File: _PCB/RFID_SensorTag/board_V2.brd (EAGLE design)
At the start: 95 x 60 mm, 21 parts, among them J2 SMT, J3 SMT, U1 MAXIM_ELECTRONICS_MAX40200AUK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, X1 53048-02

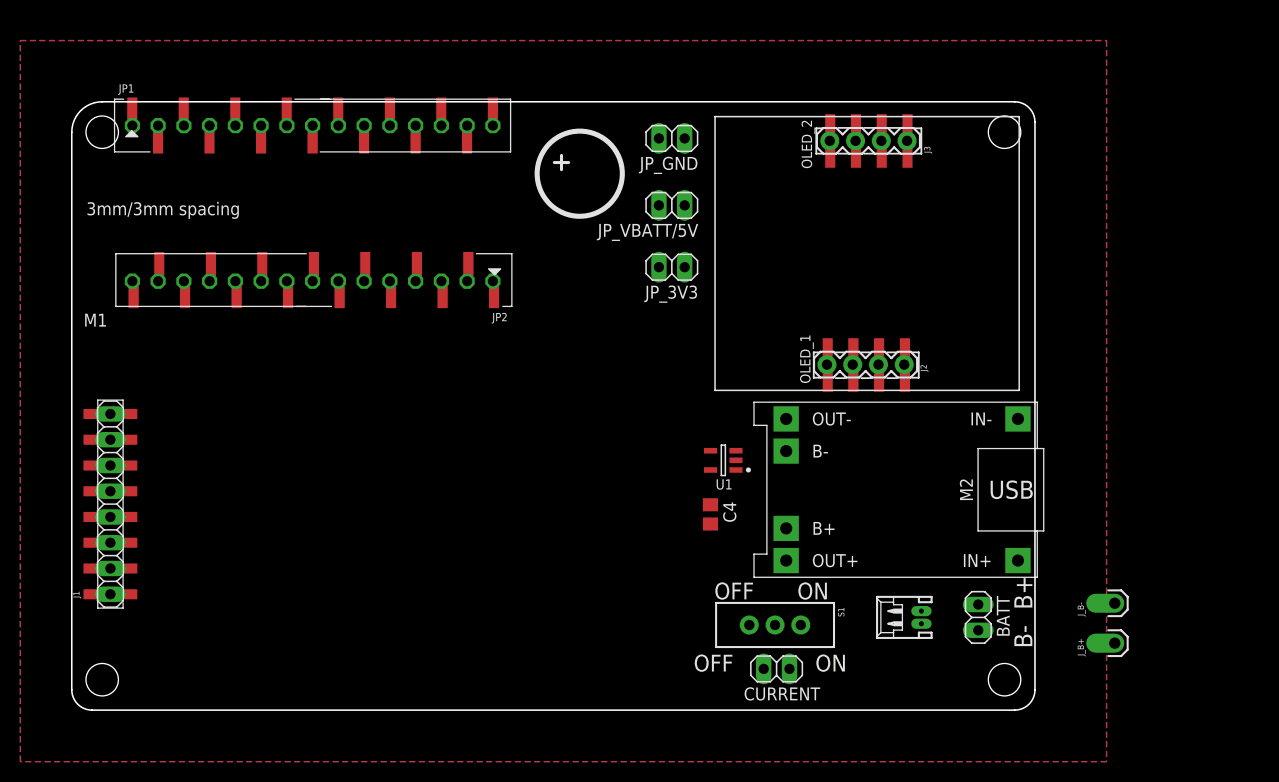
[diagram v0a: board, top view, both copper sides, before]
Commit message: RFID system V2 out
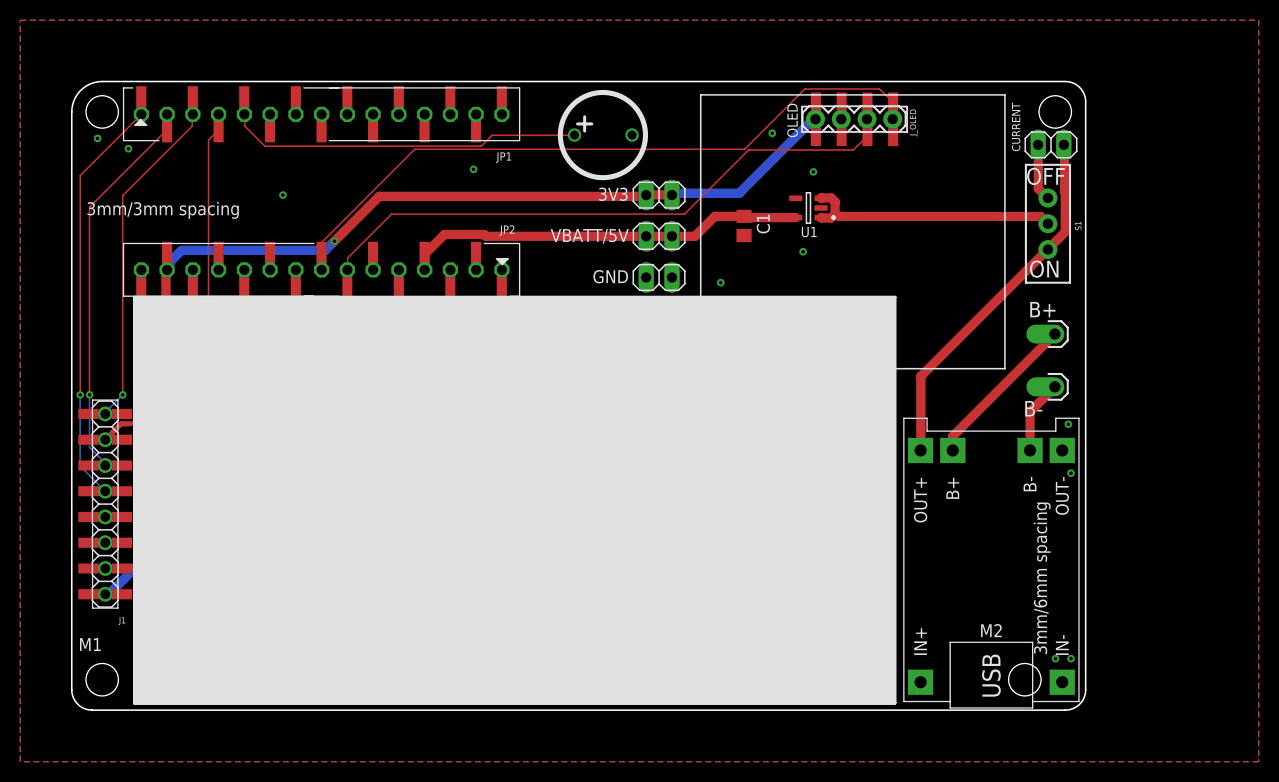
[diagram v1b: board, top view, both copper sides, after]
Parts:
- removed BATT, JP_3V3, JP_GND, JP_VBATT/5V: (no value), pinhead:1X02
- removed C4: 100nF, rcl:C0805
- removed J2, J3: SMT, SparkFun-Connectors:1X04_SMD_VERTICAL_COMBO
- removed J_B+, J_B-: (no value), SparkFun-Connectors:1X01_OFFSET
- removed OLED_1, OLED_2: (no value), SparkFun-Connectors:1X04
- removed X1: 53048-02, con-molex:53048-02
- added 3V3, GND, VBATT/5V: (no value), pinhead:1X02
- added B+, B-: (no value), SparkFun-Connectors:1X01_OFFSET
- added C1: 100nF, rcl:C0805
- added J_OLED: SMT, SparkFun-Connectors:1X04_SMD_VERTICAL_COMBO
- added OLED: (no value), SparkFun-Connectors:1X04
- moved CURRENT 58.3 mm to (96.6, 55.8)
- moved S1 47.9 mm to (96.3, 48.0), turned to 180 degrees
- moved U1 26.3 mm to (72.7, 49.5)
- moved M2 11.7 mm to (90.7, 14.8), turned to 90 degrees
- moved JP1 1.42 mm to (24.6, 58.8)
- moved U$1 1.42 mm to (33.5, 53.6)
- moved JP2 1.26 mm to (24.6, 43.4)
- moved J1 0.51 mm to (3.30, 11.4)
- moved M1 0.51 mm to (3.30, 20.3)
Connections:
- net 3.3V: now also 3V3.1, 3V3.2, JP2.14, J_OLED.4, OLED.4; no longer J2.3, J3.4, JP_3V3.1, JP_3V3.2, OLED_1.3, OLED_2.4
- net GND: now also C1.2, GND.1, GND.2, JP1.12, JP2.2, J_OLED.3, OLED.3, U$1.GND1; no longer C4.2, J2.4, J3.3, JP_GND.1, JP_GND.2, OLED_1.4, OLED_2.3
- net I2C_SCL: now also J_OLED.2, OLED.2; no longer J2.2, J3.2, OLED_1.2, OLED_2.2
- net I2C_SDA: now also J_OLED.1, OLED.1; no longer J2.1, J3.1, OLED_1.1, OLED_2.1
- net N$1: now also B+.1; no longer BATT.1, J_B+.1, X1.1
- net N$5: now also B-.1; no longer BATT.2, J_B-.1, X1.2
- net V_BATT: now also C1.1, JP2.4, VBATT/5V.1, VBATT/5V.2; no longer C4.1, JP_VBATT/5V.1, JP_VBATT/5V.2
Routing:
- net 3.3V: track 0.00 -> 110.0 mm, vias 0 -> 2
- net I2C_SDA: track 0.00 -> 67.6 mm
- net I2C_SCL: track 0.00 -> 62.4 mm
- net RFID_RST: track 0.00 -> 53.3 mm
- net SPI_MISO: track 0.00 -> 43.9 mm, vias 0 -> 1
- net SPI_MOSI: track 0.00 -> 40.1 mm, vias 0 -> 1
- net V_BATT: track 0.00 -> 39.9 mm
- net BUZZER: track 0.00 -> 36.5 mm, vias 0 -> 1
- net SPI_SS: track 0.00 -> 36.4 mm, vias 0 -> 1
- net N$2: track 0.00 -> 36.1 mm
- net BATT_VOUT: track 0.00 -> 25.7 mm
- net SPI_SCK: track 0.00 -> 20.4 mm
- net N$1: track 0.00 -> 15.6 mm
- net N$5: track 0.00 -> 7.29 mm
- net N$4: track 0.00 -> 5.65 mm
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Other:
- board size 95 x 60 mm -> 100 x 62 mm
- board text added: "3mm/6mm spacing"
- board text removed: "B+"
- board text removed: "B-"
